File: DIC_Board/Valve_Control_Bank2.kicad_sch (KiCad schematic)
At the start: 10 parts, among them U21 DRV8823QDCARQ1

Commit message: Completed Acid Pump sheet
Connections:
- net GND: no longer C214.2
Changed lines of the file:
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@@
-		)
-	)
-	(label "GND"
-		(at 171.45 69.85 270)
-		(effects
-			(font
-				(size 1.27 1.27)
-			)
-			(justify right bottom)
 		)
 	)

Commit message: Wrapping up schematic
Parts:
- removed R210, R211, R212, R213: 3.3R, Resistor_SMD:R_1206_3216Metric, symbol Device:R_Small_US
- added R332, R333, R334, R335: 3.3R, Resistor_SMD:R_0402_1005Metric, symbol Device:R
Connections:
- net GND: now also C214.2, R332.2, R333.2, R334.2, R335.2
- net at U21.21 (DISEN): now also R335.1
- net at U21.26 (CISEN): now also R334.1
- net at U21.4 (AISEN): now also R332.1
- net at U21.47 (BISEN): now also R333.1
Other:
- moved on the sheet: C210, C211, C212, C213, C214, U21

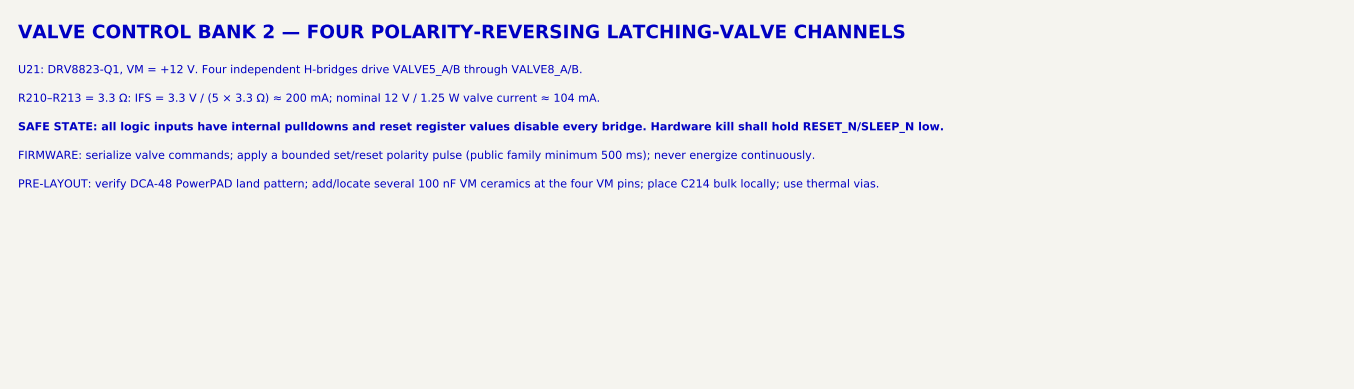
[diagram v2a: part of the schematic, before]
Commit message: Synchronize power, communications, and MCU configuration
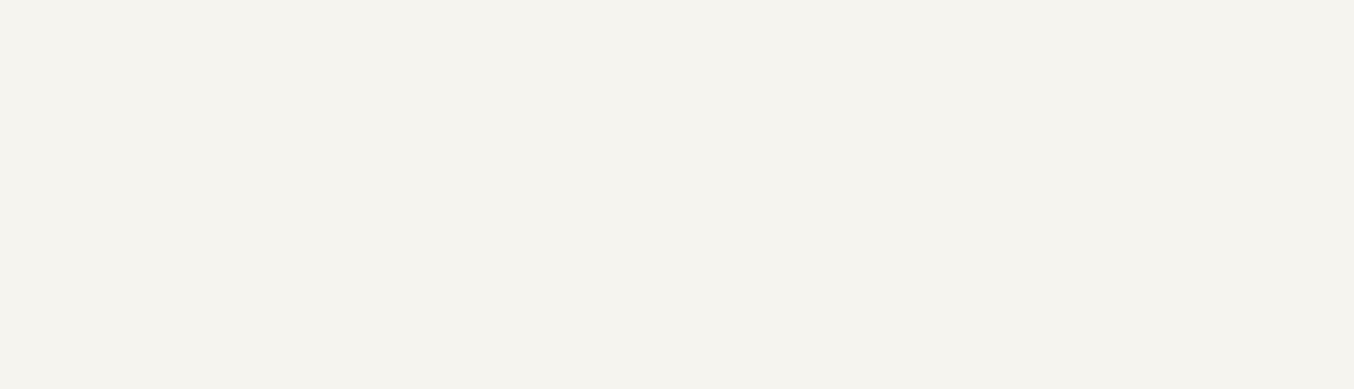
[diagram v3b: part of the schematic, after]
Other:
- note removed: "FIRMWARE: serialize valve commands; apply a bounded set/reset polarity pulse (public family minimum 500 ms); never energize continuously."
- note removed: "PRE-LAYOUT: verify DCA-48 PowerPAD land pattern; add/locate several 100 nF VM ceramics at the four VM pins; place C214 bulk locally; use thermal vias."
- note removed: "R210–R213 = 3.3 Ω: IFS = 3.3 V / (5 × 3.3 Ω) ≈ 200 mA; nominal 12 V / 1.25 W valve current ≈ 104 mA."
- note removed: "SAFE STATE: all logic inputs have internal pulldowns and reset register values disable every bridge. Hardware kill shall hold RESET_N/SLEEP_N low."
- note removed: "U21: DRV8823-Q1, VM = +12 V. Four independent H-bridges drive VALVE5_A/B through VALVE8_A/B."
- note removed: "VALVE CONTROL BANK 2 — FOUR POLARITY-REVERSING LATCHING-VALVE CHANNELS"
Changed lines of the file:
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@@
 		(comment 2 "DRV8823-Q1 serial quad H-bridge")
-	)
-	(text "VALVE CONTROL BANK 2 — FOUR POLARITY-REVERSING LATCHING-VALVE CHANNELS"
-		(exclude_from_sim no)
-		(at 25.4 20.32 0)
-		(effects
-			(font
-				(size 1.5 1.5)
-				(bold yes)
-			)
-			(justify left bottom)
-		)
-	)
-	(text "U21: DRV8823-Q1, VM = +12 V. Four independent H-bridges drive VALVE5_A/B through VALVE8_A/B."
-		(exclude_from_sim no)
-		(at 25.4 24.13 0)
-		(effects
-			(font
-				(size 0.9 0.9)
-			)
-			(justify left bottom)
-		)
-	)
-	(text "FIRMWARE: serialize valve commands; apply a bounded set/reset polarity pulse (public family minimum 500 ms); never energize continuously."
-		(exclude_from_sim no)
-		(at 25.4 33.655 0)
-		(effects
-			(font
-				(size 0.9 0.9)
-			)
-			(justify left bottom)
-		)
-	)
-	(text "PRE-LAYOUT: verify DCA-48 PowerPAD land pattern; add/locate several 100 nF VM ceramics at the four VM pins; place C214 bulk locally; use thermal vias."
-		(exclude_from_sim no)
-		(at 25.4 36.83 0)
-		(effects
-			(font
-				(size 0.9 0.9)
-			)
-			(justify left bottom)
-		)
-	)
-	(text "SAFE STATE: all logic inputs have internal pulldowns and reset register values disable every bridge. Hardware kill shall hold RESET_N/SLEEP_N low."
-		(exclude_from_sim no)
-		(at 25.4 30.48 0)
-		(effects
-			(font
-				(size 0.9 0.9)
-				(bold yes)
-			)
-			(justify left bottom)
-		)
-	)
-	(text "R210–R213 = 3.3 Ω: IFS = 3.3 V / (5 × 3.3 Ω) ≈ 200 mA; nominal 12 V / 1.25 W valve current ≈ 104 mA."
-		(exclude_from_sim no)
-		(at 25.4 27.305 0)
-		(effects
-			(font
-				(size 0.9 0.9)
-			)
-			(justify left bottom)
-		)
 	)
 	(junction

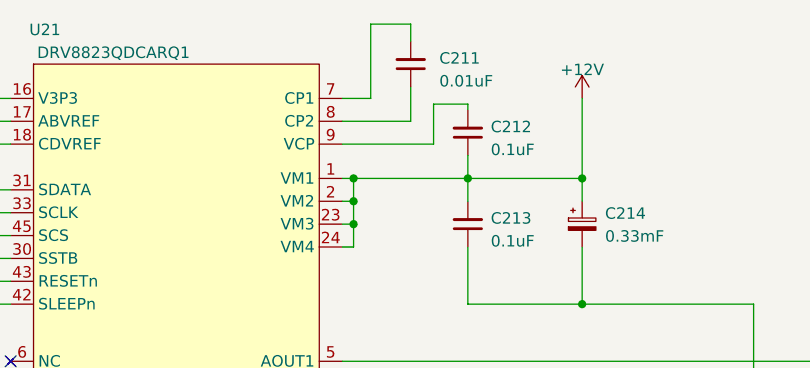
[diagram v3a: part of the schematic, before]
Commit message: Updated board for layout! All footprints added
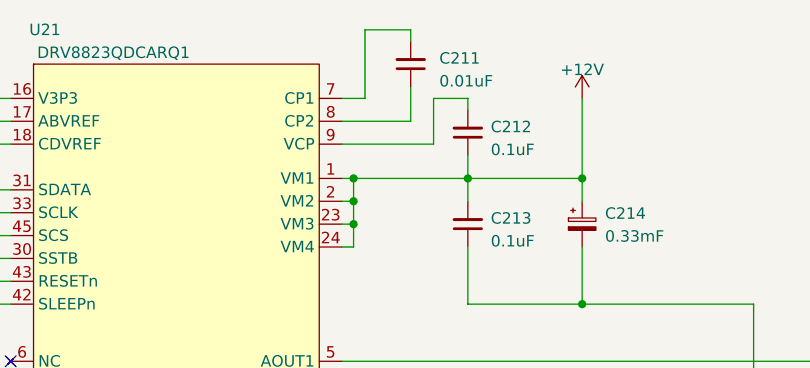
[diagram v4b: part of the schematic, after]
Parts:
- C210: Manufacturer (none) -> TDK
- C211, C212, C213: Manufacturer (none) -> KEMET
- C214: Manufacturer (none) -> Nichicon
- R332, R333, R334, R335: BOM Source (none) -> https://www.vishay.com/docs/20043/crcwhpe3.pdf; MPN (none) -> CRCW04023R30FKEDHP; Manufacturer Vishay Dale -> Vishay; Power Rating (none) -> 0.2W; Tolerance (none) -> 1%
- U21: footprint DIC_Board:HTSSOP48 -> DIC_Board:DRV8823_DCA48_ReviewFixed; Manufacturer (none) -> Texas Instruments
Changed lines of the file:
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@@
 	(wire
 		(pts
-			(xy 143.51 69.215) (xy 143.51 69.85)
+			(xy 143.51 68.58) (xy 143.51 69.85)
 		)
 		(stroke
@@
 	(wire
 		(pts
-			(xy 137.16 60.325) (xy 137.16 62.23)
+			(xy 137.16 60.96) (xy 137.16 62.23)
 		)
 		(stroke
@@
 	(wire
 		(pts
-			(xy 132.715 60.325) (xy 137.16 60.325)
+			(xy 132.08 60.96) (xy 137.16 60.96)
 		)
 		(stroke
@@
 	(wire
 		(pts
-			(xy 139.7 69.215) (xy 143.51 69.215)
+			(xy 139.7 68.58) (xy 143.51 68.58)
 		)
 		(stroke
@@
 	(wire
 		(pts
-			(xy 132.715 68.58) (xy 132.715 60.325)
-		)
-		(stroke
-			(width 0)
-			(type default)
-		)
-	)
-	(wire
-		(pts
-			(xy 129.54 68.58) (xy 132.715 68.58)
-		)
-		(stroke
-			(width 0)
-			(type default)
-		)
-	)
-	(wire
-		(pts
-			(xy 139.7 73.66) (xy 139.7 69.215)
+			(xy 132.08 68.58) (xy 132.08 60.96)
+		)
+		(stroke
+			(width 0)
+			(type default)
+		)
+	)
+	(wire
+		(pts
+			(xy 129.54 68.58) (xy 132.08 68.58)
+		)
+		(stroke
+			(width 0)
+			(type default)
+		)
+	)
+	(wire
+		(pts
+			(xy 139.7 73.66) (xy 139.7 68.58)
 		)
 		(stroke
@@
 			)
 		)
+		(property "Manufacturer" "KEMET"
+			(at 0 0 0)
+			(hide yes)
+			(show_name no)
+			(do_not_autoplace no)
+			(effects
+				(font
+					(size 1.27 1.27)
+				)
+			)
+		)
 		(pin "1"
 		)
@@
 			)
 		)
+		(property "Manufacturer" "KEMET"
+			(at 0 0 0)
+			(hide yes)
+			(show_name no)
+			(do_not_autoplace no)
+			(effects
+				(font
+					(size 1.27 1.27)
+				)
+			)
+		)
 		(pin "1"
 		)
@@
 			)
 		)
-		(property "MPN" ""
+		(property "MPN" "CRCW04023R30FKEDHP"
 			(at 138.43 133.35 0)
 			(hide yes)
@@
 			)
 		)
-		(property "Manufacturer" "Vishay Dale"
+		(property "Manufacturer" "Vishay"
 			(at 138.43 133.35 0)
+			(hide yes)
+			(show_name no)
+			(do_not_autoplace no)
+			(effects
+				(font
+					(size 1.27 1.27)
+				)
+			)
+		)
+		(property "Tolerance" "1%"
+			(at 0 0 0)
+			(hide yes)
+			(show_name no)
+			(do_not_autoplace no)
+			(effects
+				(font
+					(size 1.27 1.27)
+				)
+			)
+		)
+		(property "Power Rating" "0.2W"
+			(at 0 0 0)
+			(hide yes)
+			(show_name no)
+			(do_not_autoplace no)
+			(effects
+				(font
+					(size 1.27 1.27)
+				)
+			)
+		)
+		(property "BOM Source" "https://www.vishay.com/docs/20043/crcwhpe3.pdf"
+			(at 0 0 0)
 			(hide yes)
 			(show_name no)
@@
 			)
 		)
+		(property "Manufacturer" "TDK"
+			(at 0 0 0)
+			(hide yes)
+			(show_name no)
+			(do_not_autoplace no)
+			(effects
+				(font
+					(size 1.27 1.27)
+				)
+			)
+		)
 		(pin "1"
 		)
@@
 			)
 		)
-		(property "MPN" ""
+		(property "MPN" "CRCW04023R30FKEDHP"
 			(at 138.43 148.59 0)
 			(hide yes)
@@
 			)
 		)
-		(property "Manufacturer" "Vishay Dale"
+		(property "Manufacturer" "Vishay"
 			(at 138.43 148.59 0)
+			(hide yes)
+			(show_name no)
+			(do_not_autoplace no)
+			(effects
+				(font
+					(size 1.27 1.27)
+				)
+			)
+		)
+		(property "Tolerance" "1%"
+			(at 0 0 0)
+			(hide yes)
+			(show_name no)
+			(do_not_autoplace no)
+			(effects
+				(font
+					(size 1.27 1.27)
+				)
+			)
+		)
+		(property "Power Rating" "0.2W"
+			(at 0 0 0)
+			(hide yes)
+			(show_name no)
+			(do_not_autoplace no)
+			(effects
+				(font
+					(size 1.27 1.27)
+				)
+			)
+		)
+		(property "BOM Source" "https://www.vishay.com/docs/20043/crcwhpe3.pdf"
+			(at 0 0 0)
 			(hide yes)
 			(show_name no)
@@
 			)
 		)
-		(property "MPN" ""
+		(property "MPN" "CRCW04023R30FKEDHP"
 			(at 138.43 118.11 0)
 			(hide yes)
@@
 			)
 		)
-		(property "Manufacturer" "Vishay Dale"
+		(property "Manufacturer" "Vishay"
 			(at 138.43 118.11 0)
+			(hide yes)
+			(show_name no)
+			(do_not_autoplace no)
+			(effects
+				(font
+					(size 1.27 1.27)
+				)
+			)
+		)
+		(property "Tolerance" "1%"
+			(at 0 0 0)
+			(hide yes)
+			(show_name no)
+			(do_not_autoplace no)
+			(effects
+				(font
+					(size 1.27 1.27)
+				)
+			)
+		)
+		(property "Power Rating" "0.2W"
+			(at 0 0 0)
+			(hide yes)
+			(show_name no)
+			(do_not_autoplace no)
+			(effects
+				(font
+					(size 1.27 1.27)
+				)
+			)
+		)
+		(property "BOM Source" "https://www.vishay.com/docs/20043/crcwhpe3.pdf"
+			(at 0 0 0)
 			(hide yes)
 			(show_name no)
@@
 			)
 		)
-		(property "Footprint" "DIC_Board:HTSSOP48"
+		(property "Footprint" "DIC_Board:DRV8823_DCA48_ReviewFixed"
 			(at 100.33 72.39 0)
 			(hide yes)
@@
 		(property "MPN" "DRV8823QDCARQ1"
 			(at 95.25 64.77 0)
+			(hide yes)
+			(show_name no)
+			(do_not_autoplace no)
+			(effects
+				(font
+					(size 1.27 1.27)
+				)
+			)
+		)
+		(property "Manufacturer" "Texas Instruments"
+			(at 0 0 0)
 			(hide yes)
 			(show_name no)
@@
 		(dnp no)
 		(fields_autoplaced yes)
-		(property "Reference" "#PWR0207"
+		(property "Reference" "#PWR9004"
 			(at 156.21 72.39 0)
 			(hide yes)
@@
 			(project "DIC_Board"
 				(path "/bb0ef0df-c181-443a-843c-695cd2e0efee/4eaefdb2-a0a4-4c79-8702-5dad81347158/a60ab3bd-76d7-4549-93c3-469c7eb3b757"
-					(reference "#PWR0207")
+					(reference "#PWR9004")
 					(unit 1)
 				)
@@
 			)
 		)
+		(property "Manufacturer" "KEMET"
+			(at 0 0 0)
+			(hide yes)
+			(show_name no)
+			(do_not_autoplace no)
+			(effects
+				(font
+					(size 1.27 1.27)
+				)
+			)
+		)
 		(pin "1"
 		)
@@
 			)
 		)
+		(property "Manufacturer" "Nichicon"
+			(at 0 0 0)
+			(hide yes)
+			(show_name no)
+			(do_not_autoplace no)
+			(effects
+				(font
+					(size 1.27 1.27)
+				)
+			)
+		)
 		(pin "1"
 		)
@@
 		(dnp no)
 		(fields_autoplaced yes)
-		(property "Reference" "#PWR0201"
+		(property "Reference" "#PWR9005"
 			(at 113.03 176.53 0)
 			(hide yes)
@@
 			(project "DIC_Board"
 				(path "/bb0ef0df-c181-443a-843c-695cd2e0efee/4eaefdb2-a0a4-4c79-8702-5dad81347158/a60ab3bd-76d7-4549-93c3-469c7eb3b757"
-					(reference "#PWR0201")
+					(reference "#PWR9005")
 					(unit 1)
 				)
@@
 			)
 		)
-		(property "MPN" ""
+		(property "MPN" "CRCW04023R30FKEDHP"
 			(at 138.43 102.87 0)
 			(hide yes)
@@
 			)
 		)
-		(property "Manufacturer" "Vishay Dale"
+		(property "Manufacturer" "Vishay"
 			(at 138.43 102.87 0)
 			(hide yes)
 			(show_name no)
+			(do_not_autoplace no)
+			(effects
+				(font
+					(size 1.27 1.27)
+				)
+			)
+		)
+		(property "Tolerance" "1%"
+			(at 0 0 0)
+			(hide yes)
+			(show_name no)
+			(do_not_autoplace no)
+			(effects
+				(font
+					(size 1.27 1.27)
+				)
+			)
+		)
+		(property "Power Rating" "0.2W"
+			(at 0 0 0)
+			(hide yes)
+			(show_name no)
+			(do_not_autoplace no)
+			(effects
+				(font
+					(size 1.27 1.27)
+				)
+			)
+		)
+		(property "BOM Source" "https://www.vishay.com/docs/20043/crcwhpe3.pdf"
+			(at 0 0 0)
+			(hide yes)
+			(show_name no)

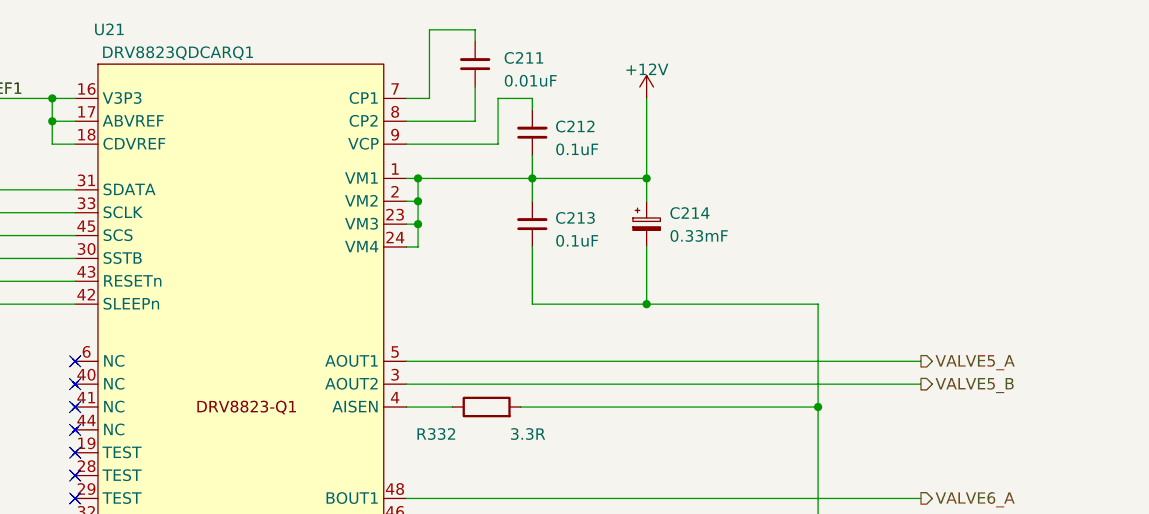
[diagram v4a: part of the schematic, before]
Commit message: Changed the 12V regulator to an integrated IC
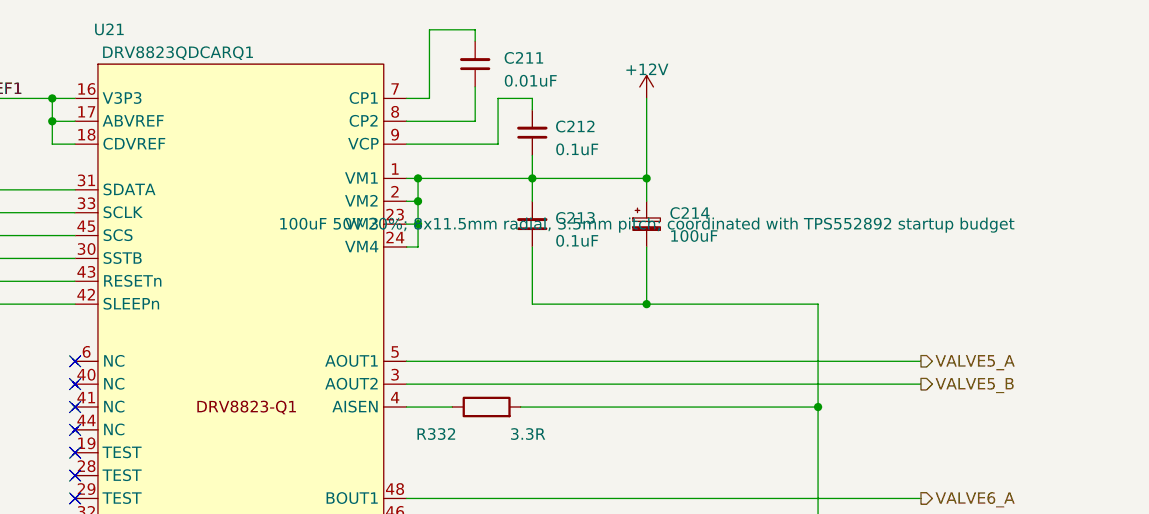
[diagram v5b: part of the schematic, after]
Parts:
- C214: value 0.33mF -> 100uF; footprint Capacitor_THT:CP_Radial_D12.5mm_P5.00mm -> Capacitor_THT:CP_Radial_D8.0mm_P3.50mm; MPN URZ1H331MHD1TO -> UHE1H101MPD
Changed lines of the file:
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@@
 			)
 		)
-		(property "Value" "0.33mF"
+		(property "Value" "100uF"
 			(at 158.75 83.9089 0)
 			(show_name no)
@@
 			)
 		)
-		(property "Footprint" "Capacitor_THT:CP_Radial_D12.5mm_P5.00mm"
+		(property "Footprint" "Capacitor_THT:CP_Radial_D8.0mm_P3.50mm"
 			(at 156.21 82.55 0)
 			(hide yes)
@@
 			)
 		)
-		(property "Datasheet" ""
+		(property "Datasheet" "https://www.nichicon.com/getmedia/5ee6e3a3-2d90-4858-bed0-89ef58a93bc3/e-uhe.pdf"
 			(at 156.21 82.55 0)
 			(hide yes)
@@
 			)
 		)
-		(property "Description" ""
+		(property "Description" "100uF 50V 20%; 8x11.5mm radial, 3.5mm pitch; coordinated with TPS552892 startup budget"
 			(at 156.21 82.55 0)
 			(show_name no)
@@
 			)
 		)
-		(property "MPN" "URZ1H331MHD1TO"
+		(property "MPN" "UHE1H101MPD"
 			(at 156.21 82.55 0)
 			(hide yes)
@@
 			(at 0 0 0)
 			(hide yes)
+			(show_name no)
+			(do_not_autoplace no)
+			(effects
+				(font
+					(size 1.27 1.27)
+				)
+			)
+		)
+		(property "Mouser" ""
+			(at 0 0 0)
+			(hide yes)
+			(show_name no)
+			(do_not_autoplace no)
+			(effects
+				(font
+					(size 1.27 1.27)
+				)
+			)
+		)
+		(property "DigiKey" ""
+			(at 0 0 0)
+			(hide yes)
